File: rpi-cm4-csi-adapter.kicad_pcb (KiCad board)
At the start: 4 copper layers, 47 x 33 mm, 19 parts, among them J1 687122149022, J2 WE_68715014522

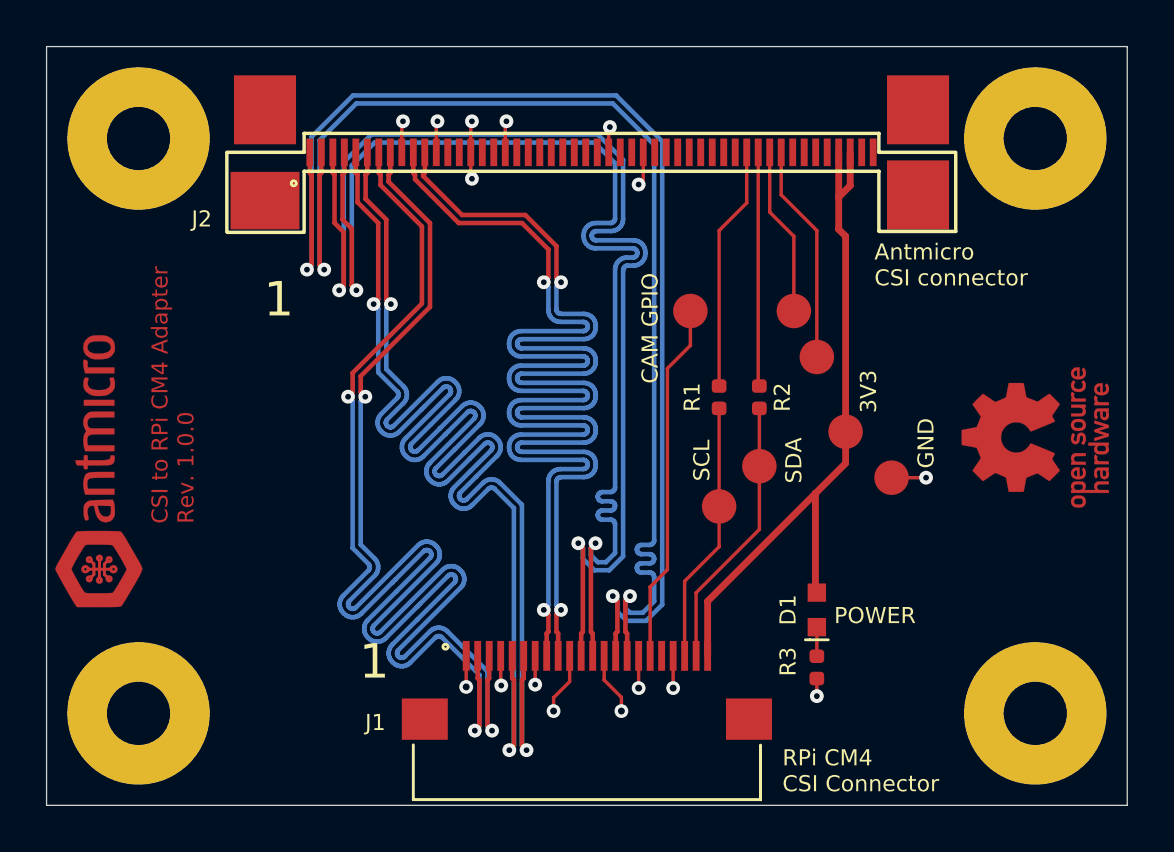
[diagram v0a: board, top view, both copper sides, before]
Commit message: Swap I2C lines - bump revision to 1.0.1
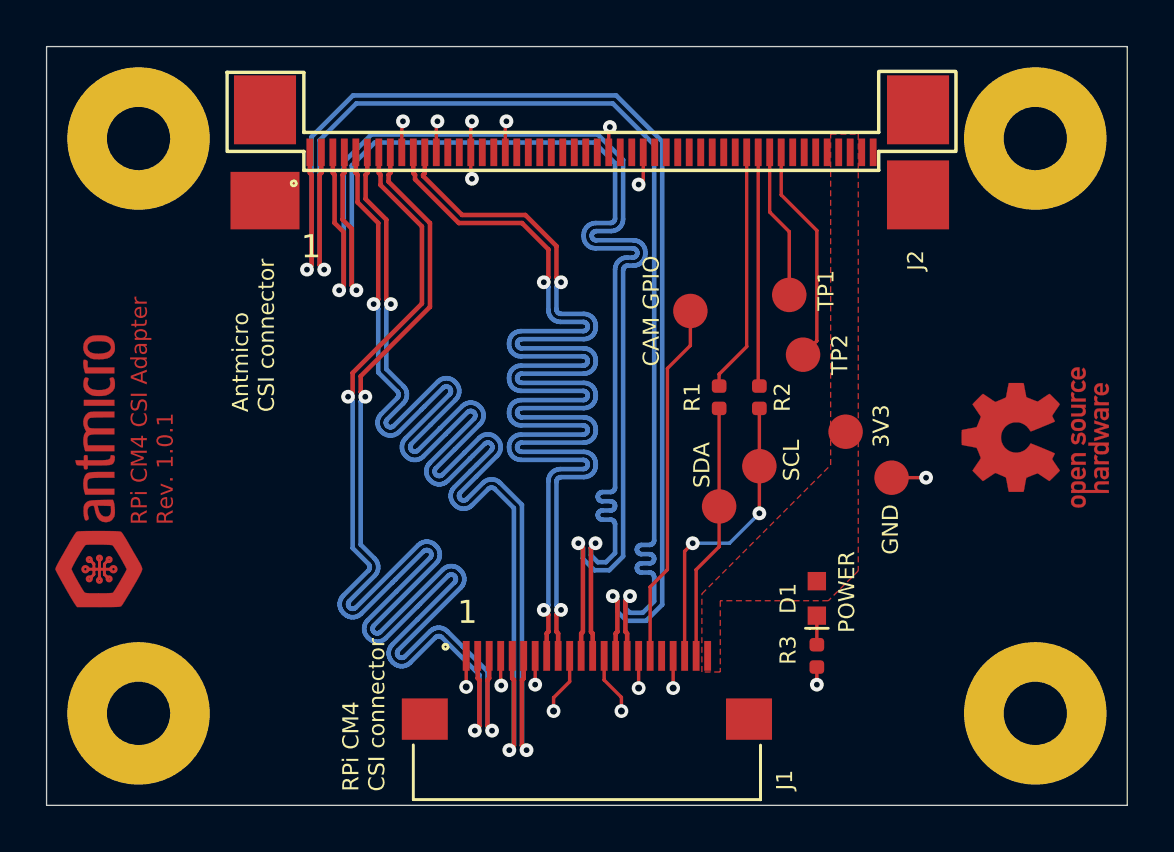
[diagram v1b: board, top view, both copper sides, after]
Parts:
- moved TP3 0.73 mm to (194.8, 63.8)
- moved TP4 0.61 mm to (195.4, 66.4)
- moved D1 0.50 mm to (196.0, 77.0)
- moved R3 0.50 mm to (196.0, 79.5)
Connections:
- J1 pad 18: Net-(J1-Pad18) -> (no net)
- J2 pad 13: Net-(J2-Pad13) -> (no net)
- J2 pad 14: Net-(J2-Pad14) -> (no net)
- J2 pad 16: Net-(J2-Pad16) -> (no net)
- J2 pad 17: Net-(J2-Pad17) -> (no net)
- J2 pad 19: Net-(J2-Pad19) -> (no net)
- J2 pad 20: Net-(J2-Pad20) -> (no net)
- J2 pad 21: Net-(J2-Pad21) -> (no net)
- J2 pad 22: Net-(J2-Pad22) -> (no net)
- J2 pad 23: Net-(J2-Pad23) -> (no net)
- J2 pad 24: Net-(J2-Pad24) -> (no net)
- J2 pad 25: Net-(J2-Pad25) -> (no net)
- J2 pad 26: Net-(J2-Pad26) -> (no net)
- J2 pad 28: Net-(J2-Pad28) -> (no net)
- J2 pad 29: Net-(J2-Pad29) -> (no net)
- J2 pad 31: Net-(J2-Pad31) -> (no net)
- J2 pad 32: Net-(J2-Pad32) -> (no net)
- J2 pad 33: Net-(J2-Pad33) -> (no net)
- J2 pad 34: Net-(J2-Pad34) -> (no net)
- J2 pad 35: Net-(J2-Pad35) -> (no net)
- J2 pad 36: Net-(J2-Pad36) -> (no net)
- J2 pad 37: Net-(J2-Pad37) -> (no net)
- J2 pad 38: Net-(J2-Pad38) -> (no net)
- J2 pad 43: Net-(J2-Pad43) -> (no net)
- J2 pad 44: Net-(J2-Pad44) -> (no net)
- J2 pad 45: Net-(J2-Pad45) -> (no net)
- J2 pad 46: Net-(J2-Pad46) -> (no net)
- J2 pad 49: Net-(J2-Pad49) -> (no net)
- J2 pad 50: Net-(J2-Pad50) -> (no net)
- R1 pad 1: /RPI_SCL0 -> /RPI_SDA0
- R2 pad 1: /RPI_SDA0 -> /RPI_SCL0
- TP1 pad 1: /RPI_SCL0 -> /RPI_SDA0
- TP2 pad 1: /RPI_SDA0 -> /RPI_SCL0
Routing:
- net VCC_3V3: track 31.0 -> 0.00 mm
- net /RPI_SCL0: track 11.4 -> 13.0 mm, vias 0 -> 2
- net /SDA2: track 7.33 -> 6.55 mm
- net /RPI_SDA0: track 11.9 -> 11.2 mm
- added copper zone on F.Cu, net VCC_3V3
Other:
- board text added: "RPi CM4 CSI Adapter Rev. 1.0.1"
- board text added: "RPi CM4 CSI connector"
- board text added: "TP1"
- board text added: "TP2"
- board text removed: "CSI to RPi CM4 Adapter Rev. 1.0.0"
- board text removed: "RPi CM4 CSI Connector"
